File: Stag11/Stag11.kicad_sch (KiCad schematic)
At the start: 2 parts

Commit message: Started work on moving connectors
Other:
- added sheet LOOM - FRONT - NEW (loom-front-new.kicad_sch)
- added sheet LOOM - REAR - NEW (loom-rear-new.kicad_sch)
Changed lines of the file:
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@@
+	)
+	(sheet
+		(at 267.97 31.75)
+		(size 25.4 21.59)
+		(fields_autoplaced yes)
+		(stroke
+			(width 0.1524)
+			(type solid)
+		)
+		(fill
+			(color 0 0 0 0.0000)
+		)
+		(property "Sheetname" "LOOM - FRONT - NEW"
+			(at 267.97 31.0384 0)
+			(effects
+				(font
+					(size 1.27 1.27)
+				)
+				(justify left bottom)
+			)
+		)
+		(property "Sheetfile" "loom-front-new.kicad_sch"
+			(at 267.97 53.9246 0)
+			(effects
+				(font
+					(size 1.27 1.27)
+				)
+				(justify left top)
+			)
+		)
+		(instances
+			(project "Stag11"
+				(path "/03011643-0690-4b85-ab78-d6a62dae52b1"
+					(page "32")
+				)
+			)
+		)
 	)
 	(sheet
@@
 				)
 			)
+		)
+	)
+	(sheet
+		(at 109.22 35.56)
+		(size 36.83 16.51)
+		(fields_autoplaced yes)
+		(stroke
+			(width 0.1524)
+			(type solid)
+		)
+		(fill
+			(color 0 0 0 0.0000)
+		)
+		(property "Sheetname" "LOOM - REAR - NEW"
+			(at 109.22 34.8484 0)
+			(effects
+				(font
+					(size 1.27 1.27)
+				)
+				(justify left bottom)
+			)
+		)
+		(property "Sheetfile" "loom-rear-new.kicad_sch"
+			(at 109.22 52.6546 0)
+			(effects
+				(font
+					(size 1.27 1.27)
+				)
+				(justify left top)
+			)
+		)
+		(instances
+			(project "Stag11"
+				(path "/03011643-0690-4b85-ab78-d6a62dae52b1"
+					(page "33")
+				)
+			)

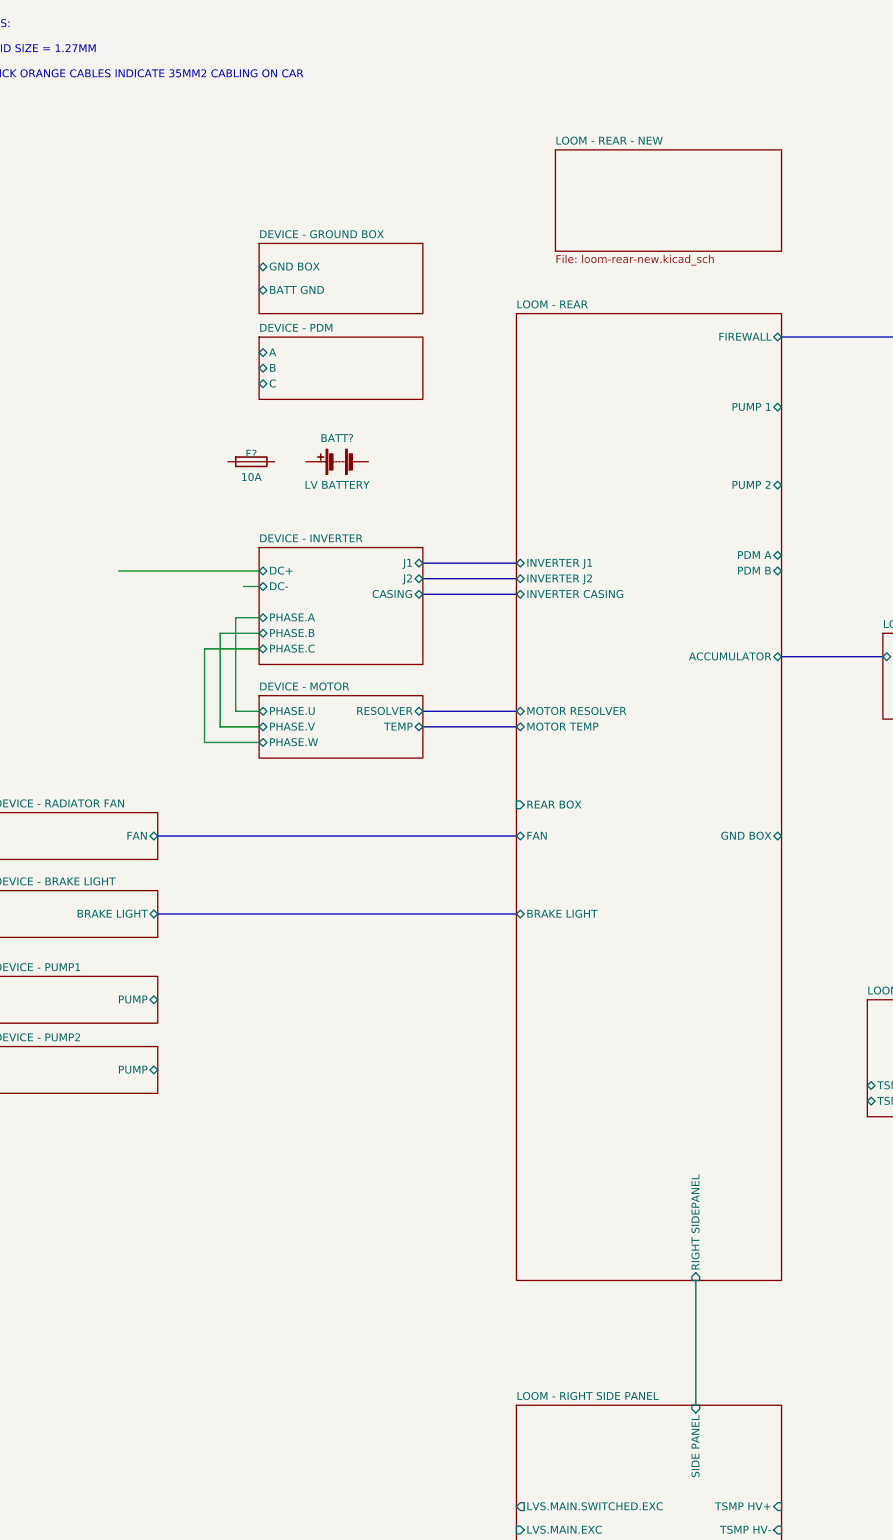
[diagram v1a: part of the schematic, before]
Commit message: Completed LV and HV Box
TODO: Spec LV connectors
TODO: Add CAN-node to LV box
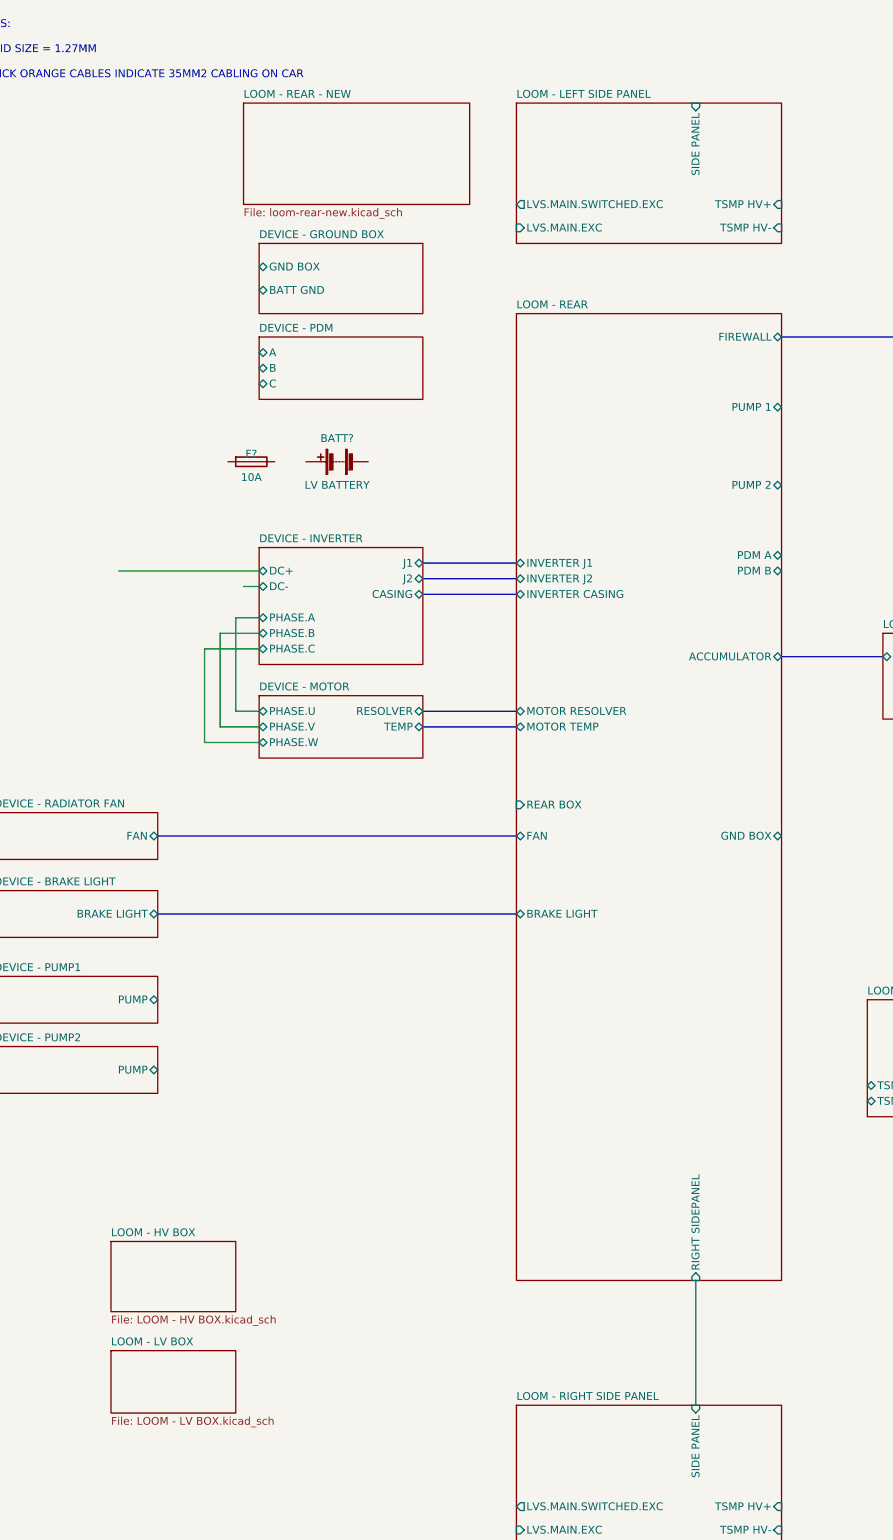
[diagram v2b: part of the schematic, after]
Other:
- added sheet LOOM - HV BOX (LOOM - HV BOX.kicad_sch)
- added sheet LOOM - LEFT SIDE PANEL (loom-side-panel.kicad_sch)
- added sheet LOOM - LV BOX (LOOM - LV BOX.kicad_sch)
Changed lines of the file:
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@@
+	)
+	(sheet
+		(at 102.87 27.94)
+		(size 43.18 22.86)
+		(fields_autoplaced yes)
+		(stroke
+			(width 0.1524)
+			(type solid)
+		)
+		(fill
+			(color 0 0 0 0.0000)
+		)
+		(property "Sheetname" "LOOM - LEFT SIDE PANEL"
+			(at 102.87 27.2284 0)
+			(effects
+				(font
+					(size 1.27 1.27)
+				)
+				(justify left bottom)
+			)
+		)
+		(property "Sheetfile" "loom-side-panel.kicad_sch"
+			(at 102.87 51.3846 0)
+			(effects
+				(font
+					(size 1.27 1.27)
+				)
+				(justify left top)
+				(hide yes)
+			)
+		)
+		(pin "LVS.MAIN.EXC" input
+			(at 102.87 48.26 180)
+			(effects
+				(font
+					(size 1.27 1.27)
+				)
+				(justify left)
+			)
+		)
+		(pin "TSMP HV-" input
+			(at 146.05 48.26 0)
+			(effects
+				(font
+					(size 1.27 1.27)
+				)
+				(justify right)
+			)
+		)
+		(pin "TSMP HV+" input
+			(at 146.05 44.45 0)
+			(effects
+				(font
+					(size 1.27 1.27)
+				)
+				(justify right)
+			)
+		)
+		(pin "SIDE PANEL" input
+			(at 132.08 27.94 90)
+			(effects
+				(font
+					(size 1.27 1.27)
+				)
+				(justify right)
+			)
+		)
+		(pin "LVS.MAIN.SWITCHED.EXC" output
+			(at 102.87 44.45 180)
+			(effects
+				(font
+					(size 1.27 1.27)
+				)
+				(justify left)
+			)
+		)
+		(instances
+			(project "Stag11"
+				(path "/03011643-0690-4b85-ab78-d6a62dae52b1"
+					(page "6")
+				)
+			)
+		)
 	)
 	(sheet
@@
 	)
 	(sheet
+		(at 36.83 231.14)
+		(size 20.32 10.16)
+		(fields_autoplaced yes)
+		(stroke
+			(width 0.1524)
+			(type solid)
+		)
+		(fill
+			(color 0 0 0 0.0000)
+		)
+		(property "Sheetname" "LOOM - LV BOX"
+			(at 36.83 230.4284 0)
+			(effects
+				(font
+					(size 1.27 1.27)
+				)
+				(justify left bottom)
+			)
+		)
+		(property "Sheetfile" "LOOM - LV BOX.kicad_sch"
+			(at 36.83 241.8846 0)
+			(effects
+				(font
+					(size 1.27 1.27)
+				)
+				(justify left top)
+			)
+		)
+		(instances
+			(project "Stag11"
+				(path "/03011643-0690-4b85-ab78-d6a62dae52b1"
+					(page "35")
+				)
+			)
+		)
+	)
+	(sheet
+		(at 36.83 213.36)
+		(size 20.32 11.43)
+		(fields_autoplaced yes)
+		(stroke
+			(width 0.1524)
+			(type solid)
+		)
+		(fill
+			(color 0 0 0 0.0000)
+		)
+		(property "Sheetname" "LOOM - HV BOX"
+			(at 36.83 212.6484 0)
+			(effects
+				(font
+					(size 1.27 1.27)
+				)
+				(justify left bottom)
+			)
+		)
+		(property "Sheetfile" "LOOM - HV BOX.kicad_sch"
+			(at 36.83 225.3746 0)
+			(effects
+				(font
+					(size 1.27 1.27)
+				)
+				(justify left top)
+			)
+		)
+		(instances
+			(project "Stag11"
+				(path "/03011643-0690-4b85-ab78-d6a62dae52b1"
+					(page "34")
+				)
+			)
+		)
+	)
+	(sheet
 		(at 342.9 62.23)
 		(size 26.67 7.62)
@@
 	)
 	(sheet
-		(at 109.22 35.56)
+		(at 58.42 27.94)
 		(size 36.83 16.51)
 		(fields_autoplaced yes)
@@
 		)
 		(property "Sheetname" "LOOM - REAR - NEW"
-			(at 109.22 34.8484 0)
+			(at 58.42 27.2284 0)
 			(effects
 				(font
@@
 		)
 		(property "Sheetfile" "loom-rear-new.kicad_sch"
-			(at 109.22 52.6546 0)
-			(effects
-				(font
+			(at 58.42 45.0346 0)
+			(effects
+				(font

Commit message: Front and Rear almost complete
TODO: Arrange power
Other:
- sheet LOOM - LEFT SIDE PANEL: file loom-side-panel.kicad_sch -> loom-side-panel-left.kicad_sch
- sheet LOOM - RIGHT SIDE PANEL: file loom-side-panel.kicad_sch -> loom-side-panel-right.kicad_sch
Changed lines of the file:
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@@
 			)
 		)
-		(property "Sheetfile" "loom-side-panel.kicad_sch"
+		(property "Sheetfile" "loom-side-panel-left.kicad_sch"
 			(at 102.87 51.3846 0)
 			(effects
@@
 			)
 		)
-		(property "Sheetfile" "loom-side-panel.kicad_sch"
+		(property "Sheetfile" "loom-side-panel-right.kicad_sch"
 			(at 102.87 263.4746 0)
 			(effects

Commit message: I forgot what I did but changed CAN layout
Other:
- note added: "Colour Coding"
- note added: "REVISION HISTORY: v1. INITIAL RELEASE"
- note added: "Regular CAN S CAN C Shutdown Shutdown Tap"
- note removed: "REVISION HISTORY: v1. INITIAL RELEASE v2. MOVED SAGL CONNECTOR TO FONT LOOM COMPLETED ACCUMULATOR AIR SHUTDOWN CONNECTIONS v3. ADDED PRECHARGE TO ACCU ADDED SECOND CAN BUS TO BMS FOR CHARGER FINALISED AIL FAN POWER"
- title: STAG X - TOP LEVEL -> STAG 11 - TOP LEVEL
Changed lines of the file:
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@@
 	(paper "A3")
 	(title_block
-		(title "STAG X - TOP LEVEL")
+		(title "STAG 11 - TOP LEVEL")
 	)
 	(bus
@@
 		)
 	)
+	(wire
+		(pts
+			(xy 16.51 40.64) (xy 22.86 40.64)
+		)
+		(stroke
+			(width 0)
+			(type default)
+			(color 155 0 0 1)
+		)
+	)
 	(bus
 		(pts
@@
 	(wire
 		(pts
+			(xy 16.51 38.1) (xy 22.86 38.1)
+		)
+		(stroke
+			(width 0)
+			(type default)
+			(color 255 0 0 1)
+		)
+	)
+	(wire
+		(pts
 			(xy 54.61 114.3) (xy 60.96 114.3)
 		)
@@
 			(type default)
 			(color 255 153 0 1)
+		)
+	)
+	(wire
+		(pts
+			(xy 16.51 33.02) (xy 22.86 33.02)
+		)
+		(stroke
+			(width 0)
+			(type default)
+			(color 0 0 255 1)
 		)
 	)
@@
 		)
 	)
+	(wire
+		(pts
+			(xy 16.51 35.56) (xy 22.86 35.56)
+		)
+		(stroke
+			(width 0)
+			(type default)
+			(color 0 0 155 1)
+		)
+	)
 	(bus
 		(pts
@@
 	(wire
 		(pts
+			(xy 16.51 30.48) (xy 22.86 30.48)
+		)
+		(stroke
+			(width 0)
+			(type default)
+		)
+	)
+	(wire
+		(pts
 			(xy 58.42 106.68) (xy 60.96 106.68)
 		)
@@
 	)
 	(rectangle
-		(start -201.93 55.88)
-		(end -52.07 226.06)
+		(start 46.99 46.99)
+		(end 196.85 228.6)
 		(stroke
 			(width 1)
@@
 			(type color)
 			(color 132 132 132 0.15)
+		)
+	)
+	(text "Colour Coding\n"
+		(exclude_from_sim no)
+		(at 20.066 27.686 0)
+		(effects
+			(font
+				(size 1.27 1.27)
+			)
 		)
 	)
@@
 		)
 	)
-	(text "                 REVISION HISTORY:\n\nv1.                INITIAL RELEASE\n\nv2.       MOVED SAGL CONNECTOR\n                      TO FONT LOOM\n\n             COMPLETED ACCUMULATOR\n          AIR SHUTDOWN CONNECTIONS\n\nv3.             ADDED PRECHARGE\n                           TO ACCU\n\n           ADDED SECOND CAN BUS TO\n                   BMS FOR CHARGER\n\n           FINALISED AIL FAN POWER"
+	(text "Regular\nCAN S\nCAN C\nShutdown\nShutdown Tap\n"
+		(exclude_from_sim no)
+		(at 24.638 35.814 0)
+		(effects
+			(font
+				(size 1.524 1.524)
+			)
+			(justify left)
+		)
+	)
+	(text "                 REVISION HISTORY:\n\nv1.                INITIAL RELEASE"
 		(exclude_from_sim no)
 		(at 406.4 13.97 0)
@@
 	(text "REAR MONOCOQUE"
 		(exclude_from_sim no)
-		(at -199.39 53.34 0)
+		(at 152.908 45.212 0)
 		(effects
 			(font
@@
 	)
 	(sheet
-		(at 60.96 66.04)
+		(at 163.83 99.06)
 		(size 26.67 10.16)
 		(fields_autoplaced yes)
@@
 		)
 		(property "Sheetname" "DEVICE - PDM"
-			(at 60.96 65.3284 0)
+			(at 163.83 98.3484 0)
 			(effects
 				(font
@@
 		)
 		(property "Sheetfile" "device-pdm.kicad_sch"
-			(at 60.96 76.7846 0)
+			(at 163.83 109.8046 0)
 			(effects
 				(font
@@
 		)
 		(pin "C" bidirectional
-			(at 60.96 73.66 180)
+			(at 163.83 106.68 180)
 			(effects
 				(font
@@
 		)
 		(pin "B" bidirectional
-			(at 60.96 71.12 180)
+			(at 163.83 104.14 180)
 			(effects
 				(font
@@
 		)
 		(pin "A" bidirectional
-			(at 60.96 68.58 180)
+			(at 163.83 101.6 180)
 			(effects
 				(font
@@
 	)
 	(sheet
-		(at 17.78 181.61)
+		(at 60.96 181.61)
 		(size 26.67 7.62)
 		(fields_autoplaced yes)
@@
 		)
 		(property "Sheetname" "DEVICE - PUMP2"
-			(at 17.78 180.8984 0)
+			(at 60.96 180.8984 0)
 			(effects
 				(font
@@
 		)
 		(property "Sheetfile" "device-pump.kicad_sch"
-			(at 17.78 189.8146 0)
+			(at 60.96 189.8146 0)
 			(effects
 				(font
@@
 		)
 		(pin "PUMP" bidirectional
-			(at 44.45 185.42 0)
+			(at 87.63 185.42 0)
 			(effects
 				(font
@@
 	)
 	(sheet
-		(at 17.78 170.18)
+		(at 60.96 170.18)
 		(size 26.67 7.62)
 		(fields_autoplaced yes)
@@
 		)
 		(property "Sheetname" "DEVICE - PUMP1"
-			(at 17.78 169.4684 0)
+			(at 60.96 169.4684 0)
 			(effects
 				(font
@@
 		)
 		(property "Sheetfile" "device-pump.kicad_sch"
-			(at 17.78 178.3846 0)
+			(at 60.96 178.3846 0)
 			(effects
 				(font
@@
 		)
 		(pin "PUMP" bidirectional
-			(at 44.45 173.99 0)
+			(at 87.63 173.99 0)
 			(effects
 				(font
@@
 	)
 	(sheet
-		(at 102.87 27.94)
+		(at 102.87 21.59)
 		(size 43.18 22.86)
 		(fields_autoplaced yes)
@@
 		)
 		(property "Sheetname" "LOOM - LEFT SIDE PANEL"
-			(at 102.87 27.2284 0)
+			(at 102.87 20.8784 0)
 			(effects
 				(font
@@
 		)
 		(property "Sheetfile" "loom-side-panel-left.kicad_sch"
-			(at 102.87 51.3846 0)
+			(at 102.87 45.0346 0)
 			(effects
 				(font
@@
 		)
 		(pin "LVS.MAIN.EXC" input
-			(at 102.87 48.26 180)
+			(at 102.87 41.91 180)
 			(effects
 				(font
@@
 		)
 		(pin "TSMP HV-" input
-			(at 146.05 48.26 0)
+			(at 146.05 41.91 0)
 			(effects
 				(font
@@
 		)
 		(pin "TSMP HV+" input
-			(at 146.05 44.45 0)
+			(at 146.05 38.1 0)
 			(effects
 				(font
@@
 		)
 		(pin "SIDE PANEL" input
-			(at 132.08 27.94 90)
+			(at 132.08 21.59 90)
 			(effects
 				(font
@@
 		)
 		(pin "LVS.MAIN.SWITCHED.EXC" output
-			(at 102.87 44.45 180)
+			(at 102.87 38.1 180)
 			(effects
 				(font
@@
 	)
 	(sheet
-		(at 36.83 231.14)
+		(at 161.29 152.4)
 		(size 20.32 10.16)
 		(fields_autoplaced yes)
@@
 		)
 		(property "Sheetname" "LOOM - LV BOX"
-			(at 36.83 230.4284 0)
+			(at 161.29 151.6884 0)
 			(effects
 				(font
@@
 		)
 		(property "Sheetfile" "LOOM - LV BOX.kicad_sch"
-			(at 36.83 241.8846 0)
+			(at 161.29 163.1446 0)
 			(effects
 				(font
@@
 	)
 	(sheet
-		(at 36.83 213.36)
+		(at 162.56 133.35)
 		(size 20.32 11.43)
 		(fields_autoplaced yes)
@@
 		)
 		(property "Sheetname" "LOOM - HV BOX"
-			(at 36.83 212.6484 0)
+			(at 162.56 132.6384 0)
 			(effects
 				(font
@@
 		)
 		(property "Sheetfile" "LOOM - HV BOX.kicad_sch"
-			(at 36.83 225.3746 0)
+			(at 162.56 145.3646 0)
 			(effects
 				(font
@@
 	)
 	(sheet
-		(at 60.96 50.8)
+		(at 163.83 78.74)
 		(size 26.67 11.43)
 		(fields_autoplaced yes)
@@
 		)
 		(property "Sheetname" "DEVICE - GROUND BOX"
-			(at 60.96 50.0884 0)
+			(at 163.83 78.0284 0)
 			(effects
 				(font
@@
 		)
 		(property "Sheetfile" "device-ground-box.kicad_sch"
-			(at 60.96 62.8146 0)
+			(at 163.83 90.7546 0)
 			(effects
 				(font
@@
 		)
 		(pin "GND BOX" bidirectional
-			(at 60.96 54.61 180)
+			(at 163.83 82.55 180)
 			(effects
 				(font
@@
 		)
 		(pin "BATT GND" bidirectional
-			(at 60.96 58.42 180)
-			(effects
-				(font
+			(at 163.83 86.36 180)
+			(effects
+				(font
